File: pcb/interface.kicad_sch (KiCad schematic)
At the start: 22 parts

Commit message: Converted to Kicad10
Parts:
- J11, J2, J3, J4, J5, J6, J7, J8, JP5, TP15, TP16: value ~ -> (none)

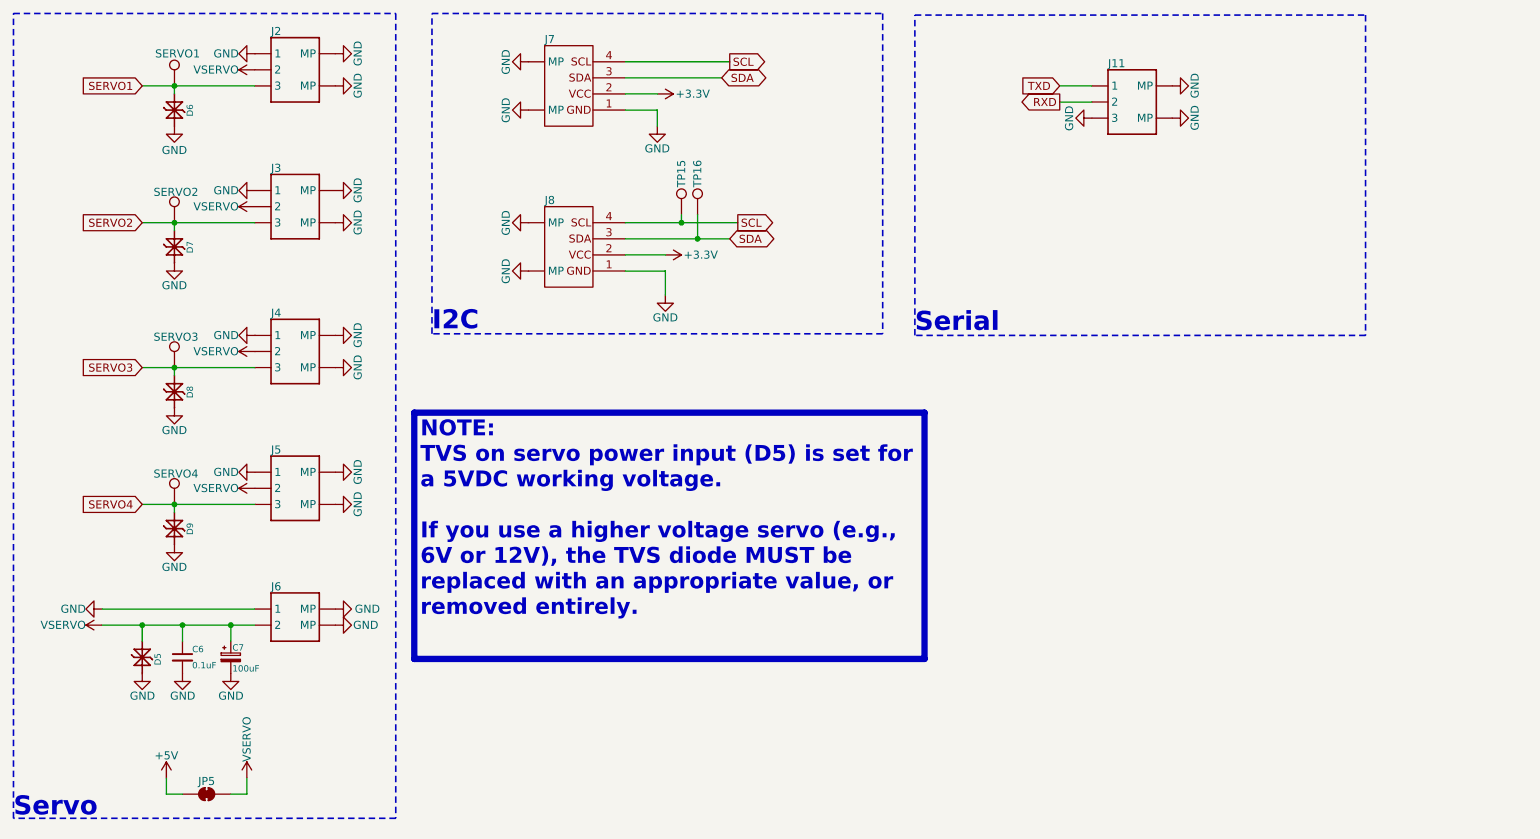
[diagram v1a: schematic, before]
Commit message: Added decoupling per servo
Updated silkscreen instructions
Refitted for guardrail
Updated renders
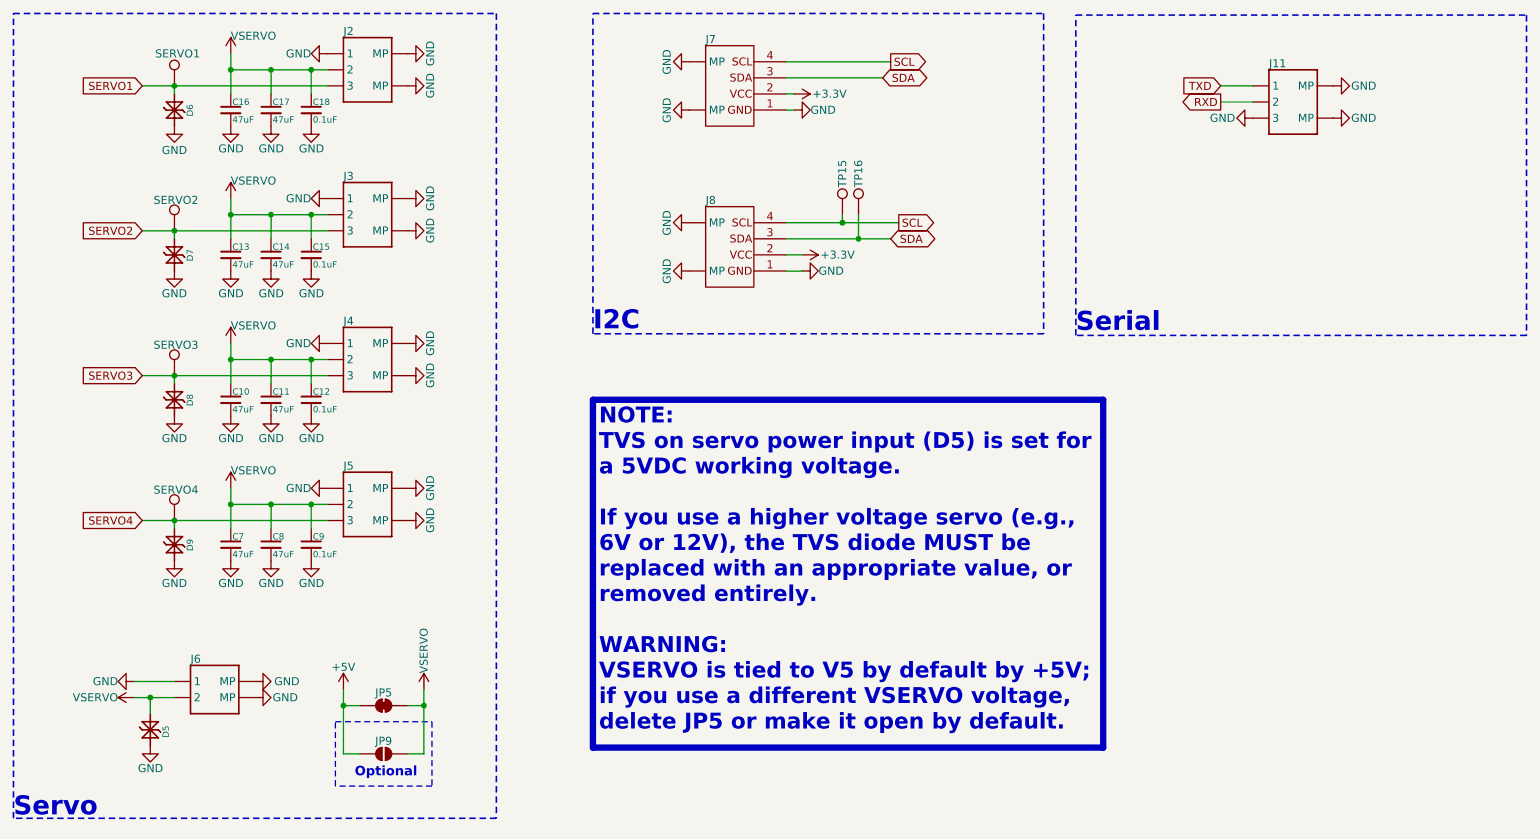
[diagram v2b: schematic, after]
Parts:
- removed C6: 0.1uF, CRGM Passive:C_0603_1608Metric, symbol Device:C_Small
- removed C7: 100uF, CRGM Passive:CP_Elec_5x5.4, symbol CRGM Passive:C_Polarized_Small
- added C10, C11, C13, C14, C16, C17, C7, C8: 47uF, CRGM Passive:C_0805_2012Metric, symbol CRGM Passive:C_Small
- added C12, C15, C18, C9: 0.1uF, CRGM Passive:C_0603_1608Metric, symbol Device:C_Small
- added JP9: (no value), CRGM Connector:SolderJumper-2_P1.3mm_Open_RoundedPad1.0x1.5mm, symbol CRGM Connector:SolderJumper_2_Open
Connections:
- net +5V: now also JP9.1 (A)
- net GND: now also C10.2, C11.2, C12.2, C13.2, C14.2, C15.2, C16.2, C17.2, C18.2, C7.2, C8.2, C9.2
- net VSERVO: now also C10.1, C11.1, C12.1, C13.1, C14.1, C15.1, C16.1, C17.1, C18.1, C7.1, C8.1, C9.1, JP9.2 (B)
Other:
- note added: "Optional"
- moved on the sheet: D5, D7, D8, D9, J11, J2, J3, J4, J5, J6, J7, J8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

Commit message: Updated symbols
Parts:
- JP5: value (none) -> SolderJumper_2_Bridged; footprint CRGM Connector:SolderJumper-2_P2.0mm_Bridged_RoundedPad1.0x1.5mm -> (none)
- JP9: value (none) -> SolderJumper_2_Open
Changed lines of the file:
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@@
 	)
 	(junction
+		(at 90.17 134.62)
+		(diameter 0)
+		(color 0 0 0 0)
+	)
+	(junction
 		(at 46.99 133.35)
 		(diameter 0)
@@
 		(color 0 0 0 0)
 	)
-	(junction
-		(at 90.17 134.62)
-		(diameter 0)
-		(color 0 0 0 0)
-	)
 	(wire
 		(pts
@@
 	(wire
 		(pts
-			(xy 90.17 134.62) (xy 87.63 134.62)
+			(xy 90.17 134.62) (xy 86.36 134.62)
 		)
 		(stroke
@@
 	(wire
 		(pts
-			(xy 87.63 142.24) (xy 90.17 142.24)
+			(xy 86.36 142.24) (xy 90.17 142.24)
 		)
 		(stroke
@@
 	(wire
 		(pts
-			(xy 77.47 134.62) (xy 80.01 134.62)
+			(xy 77.47 134.62) (xy 81.28 134.62)
 		)
 		(stroke
@@
 	(wire
 		(pts
-			(xy 80.01 142.24) (xy 77.47 142.24)
+			(xy 81.28 142.24) (xy 77.47 142.24)
 		)
 		(stroke
@@
 		(in_bom no)
 		(on_board yes)
-		(in_pos_files no)
+		(in_pos_files yes)
 		(dnp no)
 		(property "Reference" "JP5"
@@
 			)
 		)
-		(property "Value" ""
+		(property "Value" "SolderJumper_2_Bridged"
 			(at 83.82 137.16 0)
 			(hide yes)
@@
 			)
 		)
-		(property "Footprint" "CRGM Connector:SolderJumper-2_P2.0mm_Bridged_RoundedPad1.0x1.5mm"
+		(property "Footprint" ""
 			(at 83.82 134.62 0)
 			(hide yes)
@@
 			)
 		)
-		(property "LCSC" ""
-			(at 83.82 134.62 0)
-			(hide yes)
-			(show_name no)
-			(do_not_autoplace no)
-			(effects
-				(font
-					(size 1.27 1.27)
-				)
-			)
-		)
-		(property "Digikey" ""
-			(at 83.82 134.62 0)
-			(hide yes)
-			(show_name no)
-			(do_not_autoplace no)
-			(effects
-				(font
-					(size 1.27 1.27)
-				)
-			)
-		)
-		(property "Mouser" ""
-			(at 83.82 134.62 0)
-			(hide yes)
-			(show_name no)
-			(do_not_autoplace no)
-			(effects
-				(font
-					(size 1.27 1.27)
-				)
-			)
-		)
-		(property "WVDC" ""
-			(at 83.82 134.62 0)
-			(hide yes)
-			(show_name no)
-			(do_not_autoplace no)
-			(effects
-				(font
-					(size 1.27 1.27)
-				)
-			)
-		)
-		(property "MN" ""
-			(at 83.82 134.62 0)
-			(hide yes)
-			(show_name no)
-			(do_not_autoplace no)
-			(effects
-				(font
-					(size 1.27 1.27)
-				)
-			)
-		)
-		(property "MPN" ""
-			(at 83.82 134.62 0)
-			(hide yes)
-			(show_name no)
-			(do_not_autoplace no)
-			(effects
-				(font
-					(size 1.27 1.27)
-				)
-			)
-		)
 		(pin "2"
 		)
@@
 		(exclude_from_sim no)
 		(in_bom no)
-		(on_board no)
-		(in_pos_files no)
+		(on_board yes)
+		(in_pos_files yes)
 		(dnp no)
 		(property "Reference" "JP9"
@@
 			)
 		)
-		(property "Value" ""
+		(property "Value" "SolderJumper_2_Open"
 			(at 83.82 144.78 0)
 			(hide yes)
@@
 			(hide yes)
 			(show_name no)
-			(do_not_autoplace no)
-			(effects
-				(font
-					(size 1.27 1.27)
-				)
-			)
-		)
-		(property "LCSC" ""
-			(at 83.82 142.24 0)
-			(hide yes)
-			(show_name no)
-			(do_not_autoplace no)
-			(effects
-				(font
-					(size 1.27 1.27)
-				)
-			)
-		)
-		(property "Digikey" ""
-			(at 83.82 142.24 0)
-			(hide yes)
-			(show_name no)
-			(do_not_autoplace no)
-			(effects
-				(font
-					(size 1.27 1.27)
-				)
-			)
-		)
-		(property "Mouser" ""
-			(at 83.82 142.24 0)
-			(hide yes)
-			(show_name no)
-			(do_not_autoplace no)
-			(effects
-				(font
-					(size 1.27 1.27)
-				)
-			)
-		)
-		(property "WVDC" ""
-			(at 83.82 142.24 0)
-			(hide yes)
-			(show_name no)
-			(do_not_autoplace no)
-			(effects
-				(font
-					(size 1.27 1.27)
-				)
-			)
-		)
-		(property "MN" ""
-			(at 83.82 142.24 0)
-			(hide yes)
-			(show_name no)
-			(do_not_autoplace no)
-			(effects
-				(font
-					(size 1.27 1.27)
-				)
-			)
-		)
-		(property "MPN" ""
-			(at 83.82 142.24 0)
-			(hide yes)
-			(show_name no)
